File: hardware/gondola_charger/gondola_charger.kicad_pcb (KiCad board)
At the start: 2 copper layers, 41 x 23 mm, 15 parts, among them P1 board conn, Q1 Q_PMOS_GSD, U1 MCP73831T

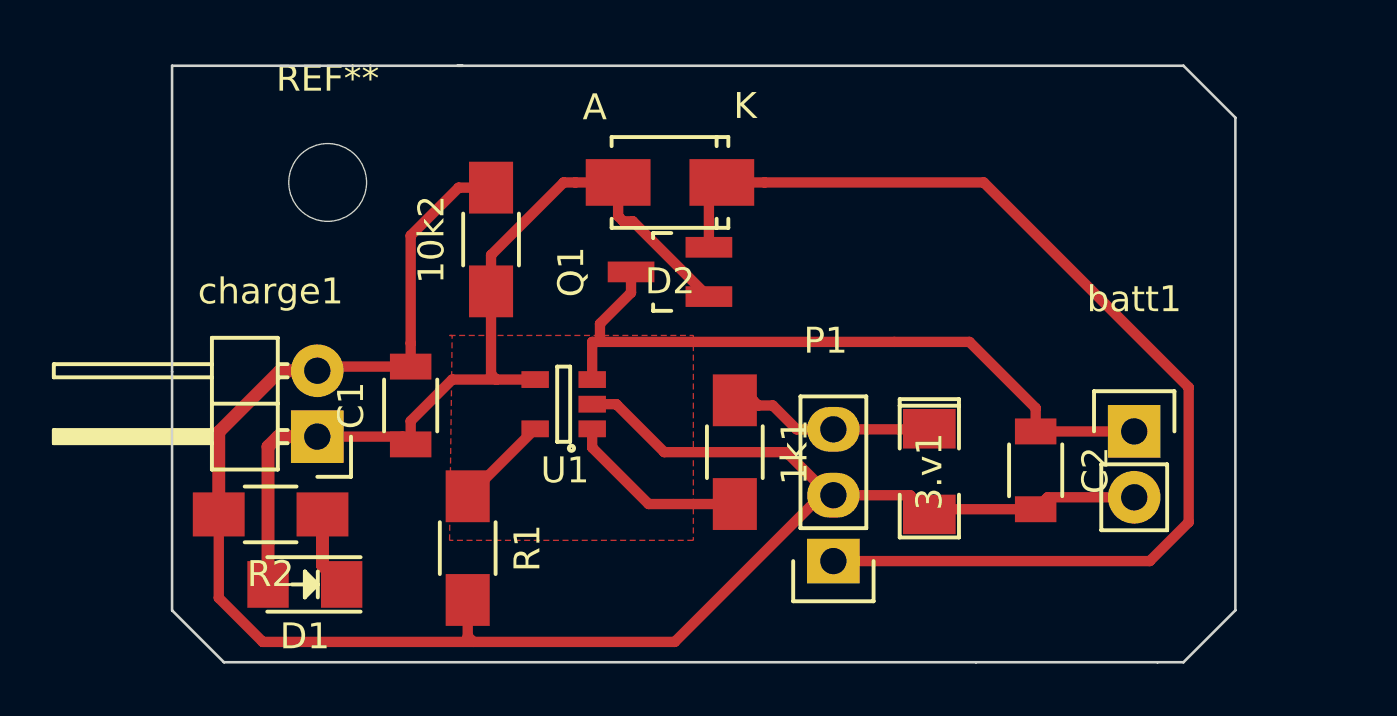
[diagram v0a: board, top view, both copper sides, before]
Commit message: mcp73832 and extra hole
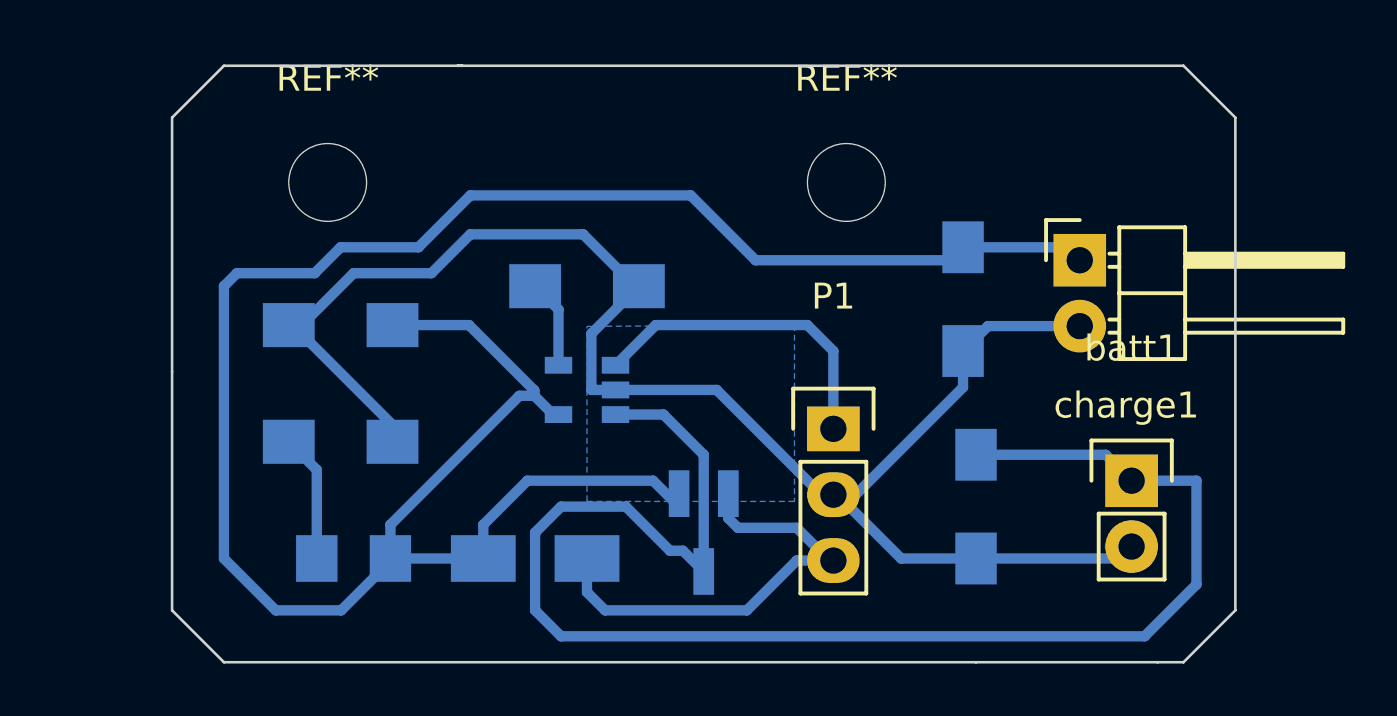
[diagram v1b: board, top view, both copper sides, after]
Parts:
- removed 10k2, 1k1: R, Resistors_SMD:R_1206_HandSoldering
- removed 3.v1: ZENER, SMD_Packages:SMD-1206_Pol
- added REF**: MountingHole_3mm, Mounting_Holes:MountingHole_3mm, F.Cu at (146.0, 98.5)
- added r1: 100k, Resistors_SMD:R_1206_HandSoldering, B.Cu at (126.5, 104.0)
- C1, C2: footprint Capacitors_SMD:C_1206 -> Capacitors_SMD:C_1206_HandSoldering; moved to B.Cu
- D1, D2, Q1, R1, R2: moved to B.Cu
- U1: value MCP73831T -> MCP73832; moved to B.Cu
- moved charge1 30.2 mm to (155.0, 101.5), turned to 0 degrees
- moved C1 21.7 mm to (150.5, 103.0), turned to 270 degrees
- moved D2 15.4 mm to (134.0, 113.0)
- moved R1 11.1 mm to (136.0, 102.5), turned to 0 degrees
- moved Q1 10.1 mm to (140.5, 112.0), turned to 0 degrees
- moved P1 5.10 mm to (145.5, 108.0), turned to 0 degrees
- moved R2 3.89 mm to (126.5, 108.5), turned to 0 degrees
- moved C2 2.69 mm to (151.0, 111.0)
- moved D1 2.13 mm to (127.0, 113.0), turned to 0 degrees
- moved batt1 1.90 mm to (157.0, 110.0)
- moved U1 1.05 mm to (136.0, 106.5)
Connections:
- P1 pad 1: powerout -> charge_safe
- P1 pad 3: charge_safe -> powerout
- U1 pad 1: Net-(1k1-Pad2) -> charge_safe
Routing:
- net +5V: track 35.3 -> 85.7 mm
- net batt: track 27.6 -> 59.6 mm
- net powerout: track 44.3 -> 17.9 mm
- net GND: track 76.2 -> 64.5 mm
- net Net-(1k1-Pad2): track 7.13 -> 0.00 mm
- net charge_safe: track 7.97 -> 12.5 mm
- net Net-(D1-Pad1): track 3.01 -> 4.95 mm
- added copper zone on B.Cu, net GND
- removed copper zone on F.Cu, net GND
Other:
- outline, holes or cut-outs redrawn
